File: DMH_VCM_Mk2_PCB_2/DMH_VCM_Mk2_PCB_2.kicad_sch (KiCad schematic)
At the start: 0 parts

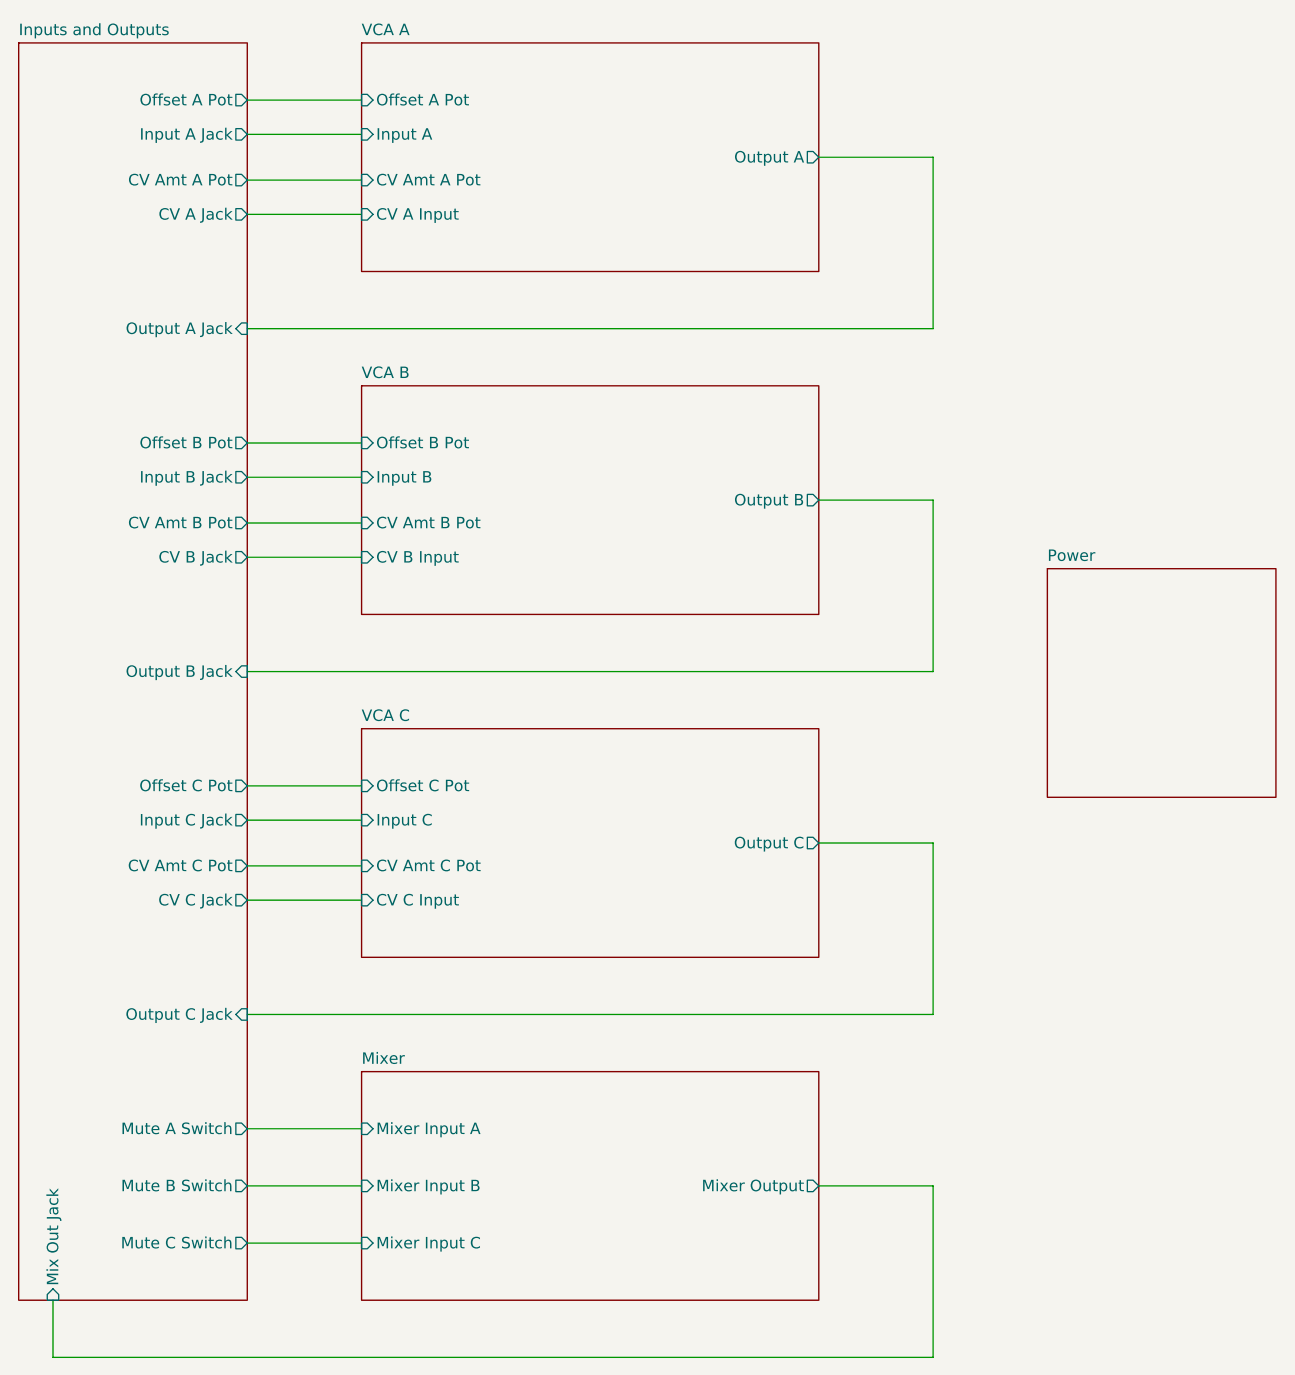
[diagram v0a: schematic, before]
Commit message: Positioned PCB 2 components
Volume conflict with headers, needs correction o PCB 1
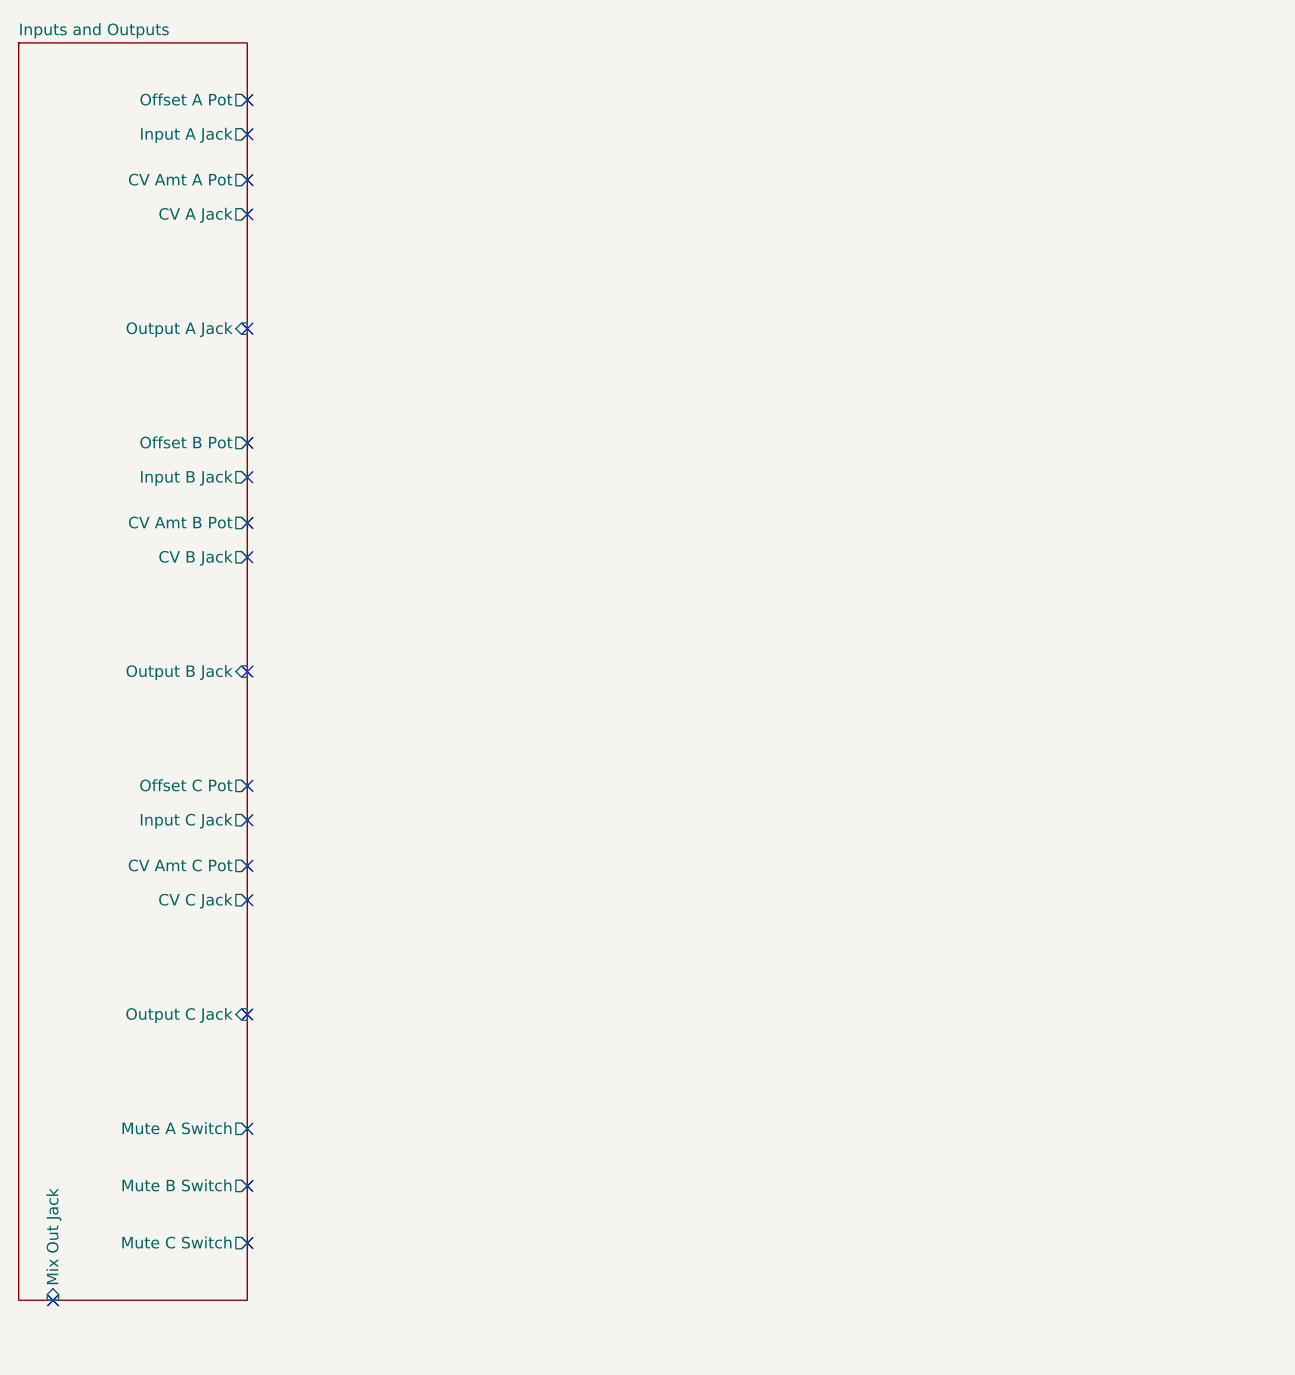
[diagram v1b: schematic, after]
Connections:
- no-connect marks 0 -> 19
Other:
- removed sheet Mixer
- removed sheet Power
- removed sheet VCA A
- removed sheet VCA B
- removed sheet VCA C
